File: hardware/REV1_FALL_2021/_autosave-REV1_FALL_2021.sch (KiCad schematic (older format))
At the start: 5 parts, among them U1 Teensy3.6_All_Pins, U2 PA16165_Breakout, U3 MPL3115A2_Breakout, U4 BNO055_Breakout, U5 RFM69HCW_Breakout

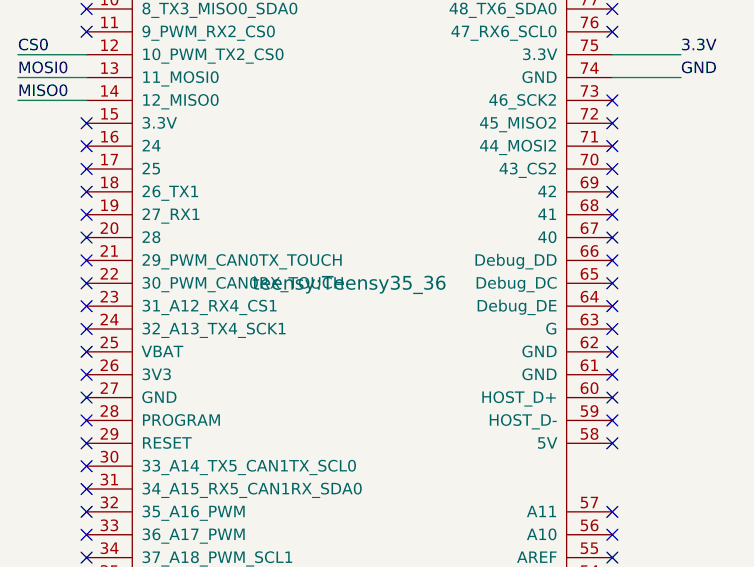
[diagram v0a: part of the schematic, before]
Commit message: Added outlines on the breakout board's footprints. Assembled PCB with wires, needs checking by Ian
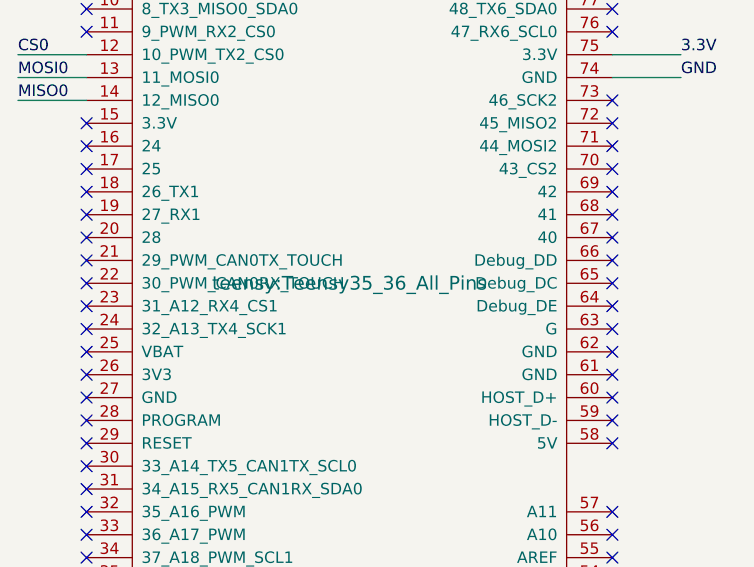
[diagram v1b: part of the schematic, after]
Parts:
- U1: footprint teensy:Teensy35_36 -> teensy:Teensy35_36_All_Pins
- U3: footprint sensors_2021_2022:MPL311A2_Breakout -> sensors_2021_2022:MPL3115A2_Breakout
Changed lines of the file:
@@
 F 0 "U1" H 2200 6237 60  0000 C CNN
 F 1 "Teensy3.6_All_Pins" H 2200 6131 60  0000 C CNN
-F 2 "teensy:Teensy35_36" H 2200 3650 60  0000 C CNN
+F 2 "teensy:Teensy35_36_All_Pins" H 2200 3650 60  0000 C CNN
 F 3 "" H 2200 3650 60  0000 C CNN
 	1    2200 3600
@@
 F 0 "U3" H 5850 4750 50  0000 L CNN
 F 1 "MPL3115A2_Breakout" H 5500 4850 50  0000 L CNN
-F 2 "sensors_2021_2022:MPL311A2_Breakout" H 5900 4400 50  0001 C CNN
+F 2 "sensors_2021_2022:MPL3115A2_Breakout" H 5900 4400 50  0001 C CNN
 F 3 "" H 5900 4400 50  0001 C CNN
 	1    5900 3950
